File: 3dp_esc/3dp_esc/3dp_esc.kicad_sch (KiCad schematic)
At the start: 12 parts, among them U1 NE555P

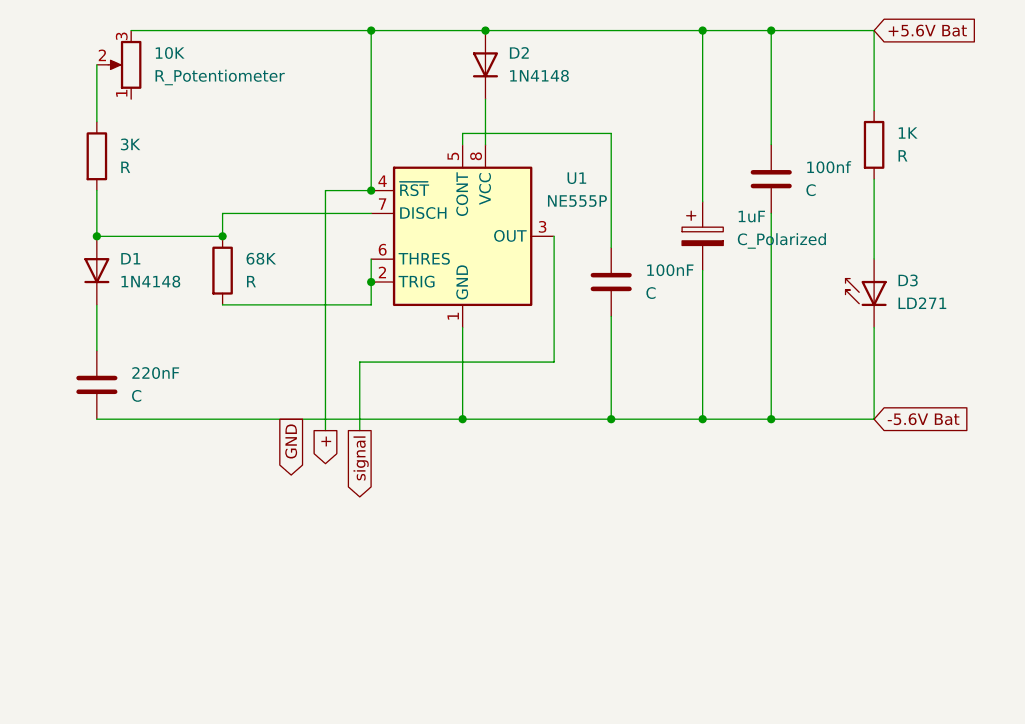
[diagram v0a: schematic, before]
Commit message: pin headers added
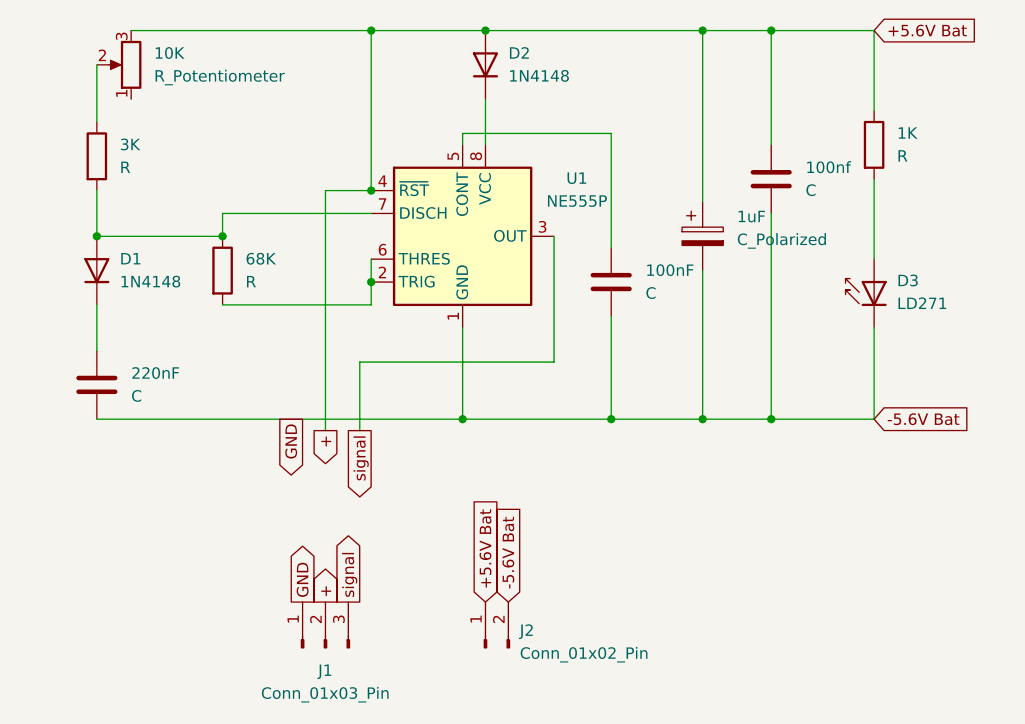
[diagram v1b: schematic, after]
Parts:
- added J1: Conn_01x03_Pin, symbol Connector:Conn_01x03_Pin
- added J2: Conn_01x02_Pin, symbol Connector:Conn_01x02_Pin
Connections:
- net +: now also J1.2 (Pin_2), J2.1 (Pin_1)
- net -5.6V Bat: now also J1.1 (Pin_1), J2.2 (Pin_2)
- net signal: now also J1.3 (Pin_3)
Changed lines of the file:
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@@
+		)
+	)
+	(global_label "+"
+		(shape output)
+		(at 121.92 142.24 90)
+		(fields_autoplaced yes)
+		(effects
+			(font
+				(size 1.27 1.27)
+			)
+			(justify left)
+		)
+		(property "Intersheetrefs" "${INTERSHEET_REFS}"
+			(at 121.92 137.6824 90)
+			(effects
+				(font
+					(size 1.27 1.27)
+				)
+				(justify left)
+				(hide yes)
+			)
+		)
+	)
+	(global_label "+5.6V Bat"
+		(shape input)
+		(at 139.7 142.24 90)
+		(fields_autoplaced yes)
+		(effects
+			(font
+				(size 1.27 1.27)
+			)
+			(justify left)
+		)
+		(property "Intersheetrefs" "${INTERSHEET_REFS}"
+			(at 139.7 129.4577 90)
+			(effects
+				(font
+					(size 1.27 1.27)
+				)
+				(justify left)
+				(hide yes)
+			)
 		)
 	)
@@
 				)
 				(justify right)
+				(hide yes)
+			)
+		)
+	)
+	(global_label "-5.6V Bat"
+		(shape input)
+		(at 142.24 142.24 90)
+		(fields_autoplaced yes)
+		(effects
+			(font
+				(size 1.27 1.27)
+			)
+			(justify left)
+		)
+		(property "Intersheetrefs" "${INTERSHEET_REFS}"
+			(at 142.24 129.4577 90)
+			(effects
+				(font
+					(size 1.27 1.27)
+				)
+				(justify left)
+				(hide yes)
+			)
+		)
+	)
+	(global_label "GND"
+		(shape output)
+		(at 119.38 142.24 90)
+		(fields_autoplaced yes)
+		(effects
+			(font
+				(size 1.27 1.27)
+			)
+			(justify left)
+		)
+		(property "Intersheetrefs" "${INTERSHEET_REFS}"
+			(at 119.38 135.3843 90)
+			(effects
+				(font
+					(size 1.27 1.27)
+				)
+				(justify left)
+				(hide yes)
+			)
+		)
+	)
+	(global_label "signal"
+		(shape output)
+		(at 124.46 142.24 90)
+		(fields_autoplaced yes)
+		(effects
+			(font
+				(size 1.27 1.27)
+			)
+			(justify left)
+		)
+		(property "Intersheetrefs" "${INTERSHEET_REFS}"
+			(at 124.46 133.5097 90)
+			(effects
+				(font
+					(size 1.27 1.27)
+				)
+				(justify left)
 				(hide yes)
 			)
@@
 	)
 	(symbol
+		(lib_id "Connector:Conn_01x03_Pin")
+		(at 121.92 147.32 90)
+		(unit 1)
+		(exclude_from_sim no)
+		(in_bom yes)
+		(on_board yes)
+		(dnp no)
+		(fields_autoplaced yes)
+		(property "Reference" "J1"
+			(at 121.92 149.86 90)
+			(effects
+				(font
+					(size 1.27 1.27)
+				)
+			)
+		)
+		(property "Value" "Conn_01x03_Pin"
+			(at 121.92 152.4 90)
+			(effects
+				(font
+					(size 1.27 1.27)
+				)
+			)
+		)
+		(property "Footprint" ""
+			(at 121.92 147.32 0)
+			(effects
+				(font
+					(size 1.27 1.27)
+				)
+				(hide yes)
+			)
+		)
+		(property "Datasheet" "~"
+			(at 121.92 147.32 0)
+			(effects
+				(font
+					(size 1.27 1.27)
+				)
+				(hide yes)
+			)
+		)
+		(property "Description" "Generic connector, single row, 01x03, script generated"
+			(at 121.92 147.32 0)
+			(effects
+				(font
+					(size 1.27 1.27)
+				)
+				(hide yes)
+			)
+		)
+		(pin "2"
+		)
+		(pin "3"
+		)
+		(pin "1"
+		)
+		(instances
+			(project ""
+				(path "/78ece2f7-d3c4-4ab2-bec9-d12b45a435bb"
+					(reference "J1")
+					(unit 1)
+				)
+			)
+		)
+	)
+	(symbol
 		(lib_id "LED:LD271")
 		(at 182.88 106.68 90)
@@
 					(unit 1)
 				)
+			)
+		)
+	)
+	(symbol
+		(lib_id "Connector:Conn_01x02_Pin")
+		(at 139.7 147.32 90)
+		(unit 1)
+		(exclude_from_sim no)
+		(in_bom yes)
+		(on_board yes)
+		(dnp no)
+		(fields_autoplaced yes)
+		(property "Reference" "J2"
+			(at 143.51 145.4149 90)
+			(effects
+				(font
+					(size 1.27 1.27)
+				)
+				(justify right)
+			)
+		)
+		(property "Value" "Conn_01x02_Pin"
+			(at 143.51 147.9549 90)
+			(effects
+				(font
+					(size 1.27 1.27)
+				)
+				(justify right)
+			)
+		)
+		(property "Footprint" ""
+			(at 139.7 147.32 0)
+			(effects
+				(font
+					(size 1.27 1.27)
+				)
+				(hide yes)
+			)
+		)
+		(property "Datasheet" "~"
+			(at 139.7 147.32 0)
+			(effects
+				(font
+					(size 1.27 1.27)
+				)
+				(hide yes)
+			)
+		)
+		(property "Description" "Generic connector, single row, 01x02, script generated"
+			(at 139.7 147.32 0)
+			(effects
+				(font
+					(size 1.27 1.27)
+				)
+				(hide yes)
+			)
+		)
+		(pin "1"
+		)
+		(pin "2"
+		)
+		(instances
+			(project ""
+				(path "/78ece2f7-d3c4-4ab2-bec9-d12b45a435bb"
+					(reference "J2")
+					(unit 1)
+				)

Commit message: Footprints added
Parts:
- 100nF, 100nf: footprint (none) -> Capacitor_THT:C_Axial_L3.8mm_D2.6mm_P7.50mm_Horizontal
- 10K: footprint (none) -> Potentiometer_THT:Potentiometer_Alps_RK163_Single_Horizontal
- 1K, 3K, 68K: footprint (none) -> Resistor_THT:R_Axial_DIN0207_L6.3mm_D2.5mm_P7.62mm_Horizontal
- 1uF: footprint (none) -> Capacitor_THT:CP_Radial_D5.0mm_P2.00mm
- 220nF: footprint (none) -> Capacitor_THT:C_Disc_D4.3mm_W1.9mm_P5.00mm
- D3: footprint LED_THT:LED_D5.0mm_IRGrey -> LED_THT:LED_D5.0mm_Clear
- J1: footprint (none) -> Connector_PinHeader_2.00mm:PinHeader_1x03_P2.00mm_Vertical
- J2: footprint (none) -> Connector_PinHeader_2.00mm:PinHeader_1x02_P2.00mm_Vertical
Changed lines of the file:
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@@
 			)
 		)
-		(property "Footprint" ""
+		(property "Footprint" "Capacitor_THT:C_Axial_L3.8mm_D2.6mm_P7.50mm_Horizontal"
 			(at 172.4152 99.06 0)
 			(effects
@@
 			)
 		)
-		(property "Footprint" ""
+		(property "Footprint" "Connector_PinHeader_2.00mm:PinHeader_1x03_P2.00mm_Vertical"
 			(at 121.92 147.32 0)
 			(effects
@@
 			)
 		)
-		(property "Footprint" "LED_THT:LED_D5.0mm_IRGrey"
+		(property "Footprint" "LED_THT:LED_D5.0mm_Clear"
 			(at 178.435 106.68 0)
 			(effects
@@
 			)
 		)
-		(property "Footprint" ""
+		(property "Footprint" "Connector_PinHeader_2.00mm:PinHeader_1x02_P2.00mm_Vertical"
 			(at 139.7 147.32 0)
 			(effects
@@
 			)
 		)
-		(property "Footprint" ""
+		(property "Footprint" "Capacitor_THT:C_Disc_D4.3mm_W1.9mm_P5.00mm"
 			(at 97.4852 121.92 0)
 			(effects
@@
 			)
 		)
-		(property "Footprint" ""
+		(property "Footprint" "Capacitor_THT:C_Axial_L3.8mm_D2.6mm_P7.50mm_Horizontal"
 			(at 154.6352 110.49 0)
 			(effects
@@
 			)
 		)
-		(property "Footprint" ""
+		(property "Footprint" "Potentiometer_THT:Potentiometer_Alps_RK163_Single_Horizontal"
 			(at 100.33 82.55 0)
 			(effects
@@
 			)
 		)
-		(property "Footprint" ""
+		(property "Footprint" "Resistor_THT:R_Axial_DIN0207_L6.3mm_D2.5mm_P7.62mm_Horizontal"
 			(at 181.102 91.44 90)
 			(effects
@@
 			)
 		)
-		(property "Footprint" ""
+		(property "Footprint" "Capacitor_THT:CP_Radial_D5.0mm_P2.00mm"
 			(at 164.7952 105.41 0)
 			(effects
@@
 			)
 		)
-		(property "Footprint" ""
+		(property "Footprint" "Resistor_THT:R_Axial_DIN0207_L6.3mm_D2.5mm_P7.62mm_Horizontal"
 			(at 108.712 105.41 90)
 			(effects
@@
 			)
 		)
-		(property "Footprint" ""
+		(property "Footprint" "Resistor_THT:R_Axial_DIN0207_L6.3mm_D2.5mm_P7.62mm_Horizontal"
 			(at 94.742 92.71 90)
 			(effects

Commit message: nets created
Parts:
- renumbered 100nF to 100nF2, 100nf to 100nf1, 10K to 10K1, 1K to 1K1, 1uF to 1uF1, 220nF to 220nF1, 3K to 3K1, 68K to 68K1, D2 to D1, D1 to D2
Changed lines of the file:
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@@
 		(dnp no)
 		(fields_autoplaced yes)
-		(property "Reference" "100nf"
+		(property "Reference" "100nf1"
 			(at 175.26 93.9799 0)
 			(effects
@@
 			(project "3dp_esc"
 				(path "/78ece2f7-d3c4-4ab2-bec9-d12b45a435bb"
-					(reference "100nf")
+					(reference "100nf1")
 					(unit 1)
 				)
@@
 		(dnp no)
 		(fields_autoplaced yes)
-		(property "Reference" "D2"
+		(property "Reference" "D1"
 			(at 142.24 81.2799 90)
 			(effects
@@
 			(project "3dp_esc"
 				(path "/78ece2f7-d3c4-4ab2-bec9-d12b45a435bb"
-					(reference "D2")
+					(reference "D1")
 					(unit 1)
 				)
@@
 		(dnp no)
 		(fields_autoplaced yes)
-		(property "Reference" "D1"
+		(property "Reference" "D2"
 			(at 99.06 104.1399 90)
 			(effects
@@
 			(project ""
 				(path "/78ece2f7-d3c4-4ab2-bec9-d12b45a435bb"
-					(reference "D1")
+					(reference "D2")
 					(unit 1)
 				)
@@
 		(dnp no)
 		(fields_autoplaced yes)
-		(property "Reference" "220nF"
+		(property "Reference" "220nF1"
 			(at 100.33 116.8399 0)
 			(effects
@@
 			(project ""
 				(path "/78ece2f7-d3c4-4ab2-bec9-d12b45a435bb"
-					(reference "220nF")
+					(reference "220nF1")
 					(unit 1)
 				)
@@
 		(dnp no)
 		(fields_autoplaced yes)
-		(property "Reference" "100nF"
+		(property "Reference" "100nF2"
 			(at 157.48 105.4099 0)
 			(effects
@@
 			(project "3dp_esc"
 				(path "/78ece2f7-d3c4-4ab2-bec9-d12b45a435bb"
-					(reference "100nF")
+					(reference "100nF2")
 					(unit 1)
 				)
@@
 		(dnp no)
 		(fields_autoplaced yes)
-		(property "Reference" "10K"
+		(property "Reference" "10K1"
 			(at 102.87 81.2799 0)
 			(effects
@@
 			(project "3dp_esc"
 				(path "/78ece2f7-d3c4-4ab2-bec9-d12b45a435bb"
-					(reference "10K")
+					(reference "10K1")
 					(unit 1)
 				)
@@
 		(dnp no)
 		(fields_autoplaced yes)
-		(property "Reference" "1K"
+		(property "Reference" "1K1"
 			(at 185.42 90.1699 0)
 			(effects
@@
 			(project "3dp_esc"
 				(path "/78ece2f7-d3c4-4ab2-bec9-d12b45a435bb"
-					(reference "1K")
+					(reference "1K1")
 					(unit 1)
 				)
@@
 		(dnp no)
 		(fields_autoplaced yes)
-		(property "Reference" "1uF"
+		(property "Reference" "1uF1"
 			(at 167.64 99.4409 0)
 			(effects
@@
 			(project ""
 				(path "/78ece2f7-d3c4-4ab2-bec9-d12b45a435bb"
-					(reference "1uF")
+					(reference "1uF1")
 					(unit 1)
 				)
@@
 		(dnp no)
 		(fields_autoplaced yes)
-		(property "Reference" "68K"
+		(property "Reference" "68K1"
 			(at 113.03 104.1399 0)
 			(effects
@@
 			(project "3dp_esc"
 				(path "/78ece2f7-d3c4-4ab2-bec9-d12b45a435bb"
-					(reference "68K")
+					(reference "68K1")
 					(unit 1)
 				)
@@
 		(dnp no)
 		(fields_autoplaced yes)
-		(property "Reference" "3K"
+		(property "Reference" "3K1"
 			(at 99.06 91.4399 0)
 			(effects
@@
 			(project ""
 				(path "/78ece2f7-d3c4-4ab2-bec9-d12b45a435bb"
-					(reference "3K")
-					(unit 1)
-				)
+					(reference "3K1")
+					(unit 1)
+				)

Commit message: i hope its fixed (it isn't)
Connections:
- net jump: now reaches 220nF1.1, D2.1 (K)
- net jump: now also 68K1.2, U1.2 (TRIG), U1.6 (THRES)
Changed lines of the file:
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@@
+	)
+	(junction
+		(at 153.67 121.92)
+		(diameter 0)
+		(color 0 0 0 0)
 	)
 	(junction
@@
 	)
 	(junction
-		(at 153.67 121.92)
-		(diameter 0)
-		(color 0 0 0 0)
-	)
-	(junction
-		(at 127 106.68)
-		(diameter 0)
-		(color 0 0 0 0)
-	)
-	(junction
 		(at 163.83 121.92)
 		(diameter 0)
@@
 	(wire
 		(pts
+			(xy 96.52 101.6) (xy 110.49 101.6)
+		)
+		(stroke
+			(width 0)
+			(type default)
+		)
+	)
+	(wire
+		(pts
+			(xy 96.52 96.52) (xy 96.52 101.6)
+		)
+		(stroke
+			(width 0)
+			(type default)
+		)
+	)
+	(wire
+		(pts
+			(xy 121.92 96.52) (xy 127 96.52)
+		)
+		(stroke
+			(width 0)
+			(type default)
+		)
+	)
+	(wire
+		(pts
+			(xy 125.73 123.19) (xy 125.73 115.57)
+		)
+		(stroke
+			(width 0)
+			(type default)
+		)
+	)
+	(wire
+		(pts
+			(xy 171.45 91.44) (xy 171.45 78.74)
+		)
+		(stroke
+			(width 0)
+			(type default)
+		)
+	)
+	(wire
+		(pts
+			(xy 139.7 78.74) (xy 163.83 78.74)
+		)
+		(stroke
+			(width 0)
+			(type default)
+		)
+	)
+	(wire
+		(pts
+			(xy 137.16 91.44) (xy 137.16 90.17)
+		)
+		(stroke
+			(width 0)
+			(type default)
+		)
+	)
+	(wire
+		(pts
+			(xy 171.45 121.92) (xy 182.88 121.92)
+		)
+		(stroke
+			(width 0)
+			(type default)
+		)
+	)
+	(wire
+		(pts
+			(xy 163.83 97.79) (xy 163.83 78.74)
+		)
+		(stroke
+			(width 0)
+			(type default)
+		)
+	)
+	(wire
+		(pts
+			(xy 127 96.52) (xy 127 78.74)
+		)
+		(stroke
+			(width 0)
+			(type default)
+		)
+	)
+	(wire
+		(pts
+			(xy 121.92 123.19) (xy 121.92 96.52)
+		)
+		(stroke
+			(width 0)
+			(type default)
+		)
+	)
+	(wire
+		(pts
+			(xy 171.45 78.74) (xy 182.88 78.74)
+		)
+		(stroke
+			(width 0)
+			(type default)
+		)
+	)
+	(wire
+		(pts
+			(xy 153.67 110.49) (xy 153.67 121.92)
+		)
+		(stroke
+			(width 0)
+			(type default)
+		)
+	)
+	(wire
+		(pts
 			(xy 96.52 109.22) (xy 96.52 114.3)
 		)
@@
 	(wire
 		(pts
-			(xy 96.52 101.6) (xy 110.49 101.6)
-		)
-		(stroke
-			(width 0)
-			(type default)
-		)
-	)
-	(wire
-		(pts
-			(xy 96.52 96.52) (xy 96.52 101.6)
-		)
-		(stroke
-			(width 0)
-			(type default)
-		)
-	)
-	(wire
-		(pts
-			(xy 121.92 96.52) (xy 127 96.52)
-		)
-		(stroke
-			(width 0)
-			(type default)
-		)
-	)
-	(wire
-		(pts
-			(xy 125.73 123.19) (xy 125.73 115.57)
-		)
-		(stroke
-			(width 0)
-			(type default)
-		)
-	)
-	(wire
-		(pts
-			(xy 171.45 91.44) (xy 171.45 78.74)
-		)
-		(stroke
-			(width 0)
-			(type default)
-		)
-	)
-	(wire
-		(pts
-			(xy 139.7 78.74) (xy 163.83 78.74)
-		)
-		(stroke
-			(width 0)
-			(type default)
-		)
-	)
-	(wire
-		(pts
-			(xy 137.16 91.44) (xy 137.16 90.17)
-		)
-		(stroke
-			(width 0)
-			(type default)
-		)
-	)
-	(wire
-		(pts
-			(xy 171.45 121.92) (xy 182.88 121.92)
-		)
-		(stroke
-			(width 0)
-			(type default)
-		)
-	)
-	(wire
-		(pts
-			(xy 163.83 97.79) (xy 163.83 78.74)
-		)
-		(stroke
-			(width 0)
-			(type default)
-		)
-	)
-	(wire
-		(pts
-			(xy 127 96.52) (xy 127 78.74)
-		)
-		(stroke
-			(width 0)
-			(type default)
-		)
-	)
-	(wire
-		(pts
-			(xy 121.92 123.19) (xy 121.92 96.52)
-		)
-		(stroke
-			(width 0)
-			(type default)
-		)
-	)
-	(wire
-		(pts
-			(xy 127 106.68) (xy 127 109.22)
-		)
-		(stroke
-			(width 0)
-			(type default)
-		)
-	)
-	(wire
-		(pts
-			(xy 171.45 78.74) (xy 182.88 78.74)
-		)
-		(stroke
-			(width 0)
-			(type default)
-		)
-	)
-	(wire
-		(pts
-			(xy 153.67 110.49) (xy 153.67 121.92)
-		)
-		(stroke
-			(width 0)
-			(type default)
-		)
-	)
-	(wire
-		(pts
 			(xy 96.52 82.55) (xy 96.52 88.9)
 		)
@@
 		(pts
 			(xy 125.73 115.57) (xy 147.32 115.57)
-		)
-		(stroke
-			(width 0)
-			(type default)
-		)
-	)
-	(wire
-		(pts
-			(xy 110.49 109.22) (xy 127 109.22)
 		)
 		(stroke
@@
 		)
 	)
+	(global_label "jump"
+		(shape input)
+		(at 127 106.68 180)
+		(fields_autoplaced yes)
+		(effects
+			(font
+				(size 1.27 1.27)
+			)
+			(justify right)
+		)
+		(property "Intersheetrefs" "${INTERSHEET_REFS}"
+			(at 119.4187 106.68 0)
+			(effects
+				(font
+					(size 1.27 1.27)
+				)
+				(justify right)
+				(hide yes)
+			)
+		)
+	)
 	(global_label "signal"
 		(shape output)
@@
 				(hide yes)
 			)
+		)
+	)
+	(global_label "jump"
+		(shape input)
+		(at 96.52 109.22 180)
+		(fields_autoplaced yes)
+		(effects
+			(font
+				(size 1.27 1.27)
+			)
+			(justify right)
+		)
+		(property "Intersheetrefs" "${INTERSHEET_REFS}"
+			(at 88.9387 109.22 0)
+			(effects
+				(font
+					(size 1.27 1.27)
+				)
+				(justify right)
+				(hide yes)
+			)
+		)
+	)
+	(global_label "jump"
+		(shape input)
+		(at 110.49 109.22 270)
+		(fields_autoplaced yes)
+		(effects
+			(font
+				(size 1.27 1.27)
+			)
+			(justify right)
+		)
+		(property "Intersheetrefs" "${INTERSHEET_REFS}"
+			(at 110.49 116.8013 90)
+			(effects
+				(font
+					(size 1.27 1.27)
+				)
+				(justify right)
+				(hide yes)
+			)

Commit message: this is good
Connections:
- net +: now also J2.2 (Pin_2); no longer J2.1 (Pin_1)
- net -5.6V Bat: now also J2.1 (Pin_1); no longer J2.2 (Pin_2)
- net jump: no longer names the net of 68K1.2, D2.1 (K), U1.2 (TRIG), U1.6 (THRES)
- net jump: no longer 220nF1.1
